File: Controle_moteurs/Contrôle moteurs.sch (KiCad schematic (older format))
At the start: 70 parts, among them P1 CONN_1, P10 CONN_1, P11 CONN_2, P12 CONN_2, P13 CONN_2, P14 CONN_2, P15 CONN_2, P16 CONN_2, P17 CONN_4, P18 CONN_5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

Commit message: Modification du connecteur de programmation
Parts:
- removed P16: CONN_2, symbol CONN_2
- removed P20: CONN_6, symbol CONN_6
- added P20, P21: CONN_5, symbol CONN_5
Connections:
- no-connect marks 0 -> 2
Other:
- note removed: "Connecteur debuggage"
- moved on the sheet: P9

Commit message: Renommé DEBUG_1/2 en TX et RX
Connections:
- net DEBUG_1 renamed DEBUG_TX
- net DEBUG_2 renamed DEBUG_RX
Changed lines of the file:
@@
-EESchema Schematic File Version 2  date 30/01/2018 12:00:08
+EESchema Schematic File Version 2  date 30/01/2018 14:31:43
 LIBS:power
 LIBS:device
@@
 $EndComp
 Text Label 10250 5850 2    60   ~ 0
-DEBUG_2
+DEBUG_RX
 Text Label 10250 5750 2    60   ~ 0
-DEBUG_1
+DEBUG_TX
 Text Notes 2200 6700 0    60   ~ 0
 Témoins d'alimentation
@@
 Need détrompeurs\nPlusieurs capas au lieu d'1 grosse
 Text Label 10400 3550 2    60   ~ 0
-DEBUG_2
+DEBUG_RX
 Text Label 10400 3450 2    60   ~ 0
-DEBUG_1
+DEBUG_TX
 Text Label 10400 4150 2    60   ~ 0
 RB4

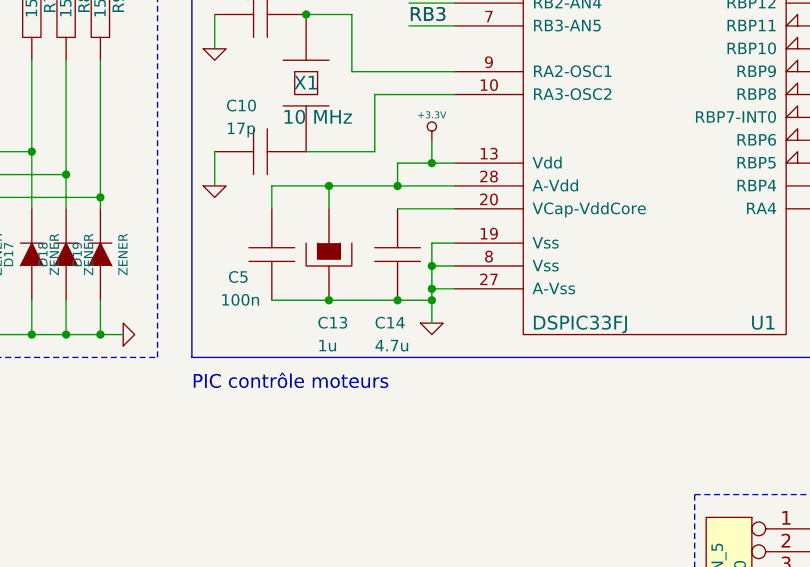
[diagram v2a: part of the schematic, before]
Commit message: Correctif : condensateur 4.7u n'était pas en polarisé
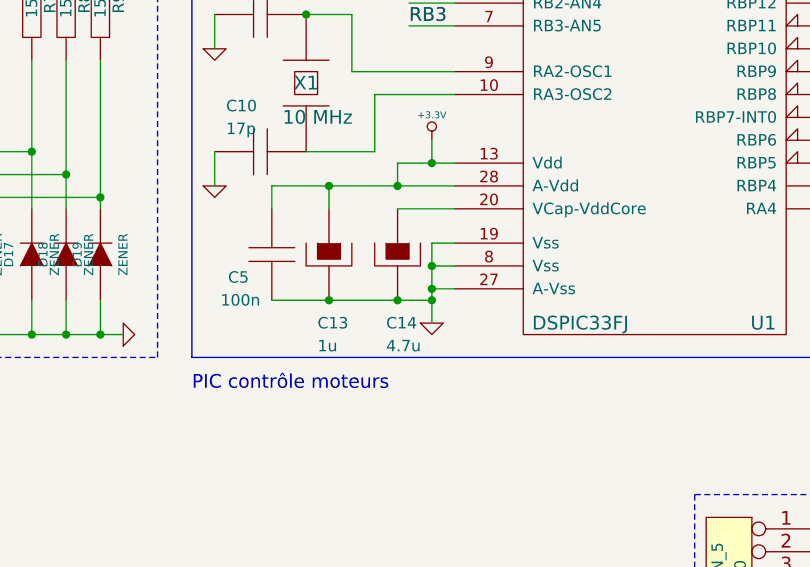
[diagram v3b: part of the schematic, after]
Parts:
- removed C14: 4.7u, symbol C
- added C14: 4.7u, symbol CAPAPOL
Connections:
- net GND: now also C14.2
- net at U1.20 (VCap-VddCore): now also C14.1
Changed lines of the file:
@@
-EESchema Schematic File Version 2  date 30/01/2018 14:31:43
+EESchema Schematic File Version 2  date 30/01/2018 16:42:31
 LIBS:power
 LIBS:device
@@
 Comment4 ""
 $EndDescr
+$Comp
+L CAPAPOL C14
+U 1 1 5A709251
+P 7900 4450
+F 0 "C14" H 7850 4150 50  0000 L CNN
+F 1 "4.7u" H 7850 4050 50  0000 L CNN
+	1    7900 4450
+	1    0    0    -1
+$EndComp
 Connection ~ 3700 1550
 Wire Wire Line
@@
 	1    0    0    -1
 $EndComp
-$Comp
-L C C14
-U 1 1 4BFD3B62
-P 7900 4450
-F 0 "C14" H 7800 4150 50  0000 L CNN
-F 1 "4.7u" H 7800 4050 50  0000 L CNN
-	1    7900 4450
-	1    0    0    -1
-$EndComp

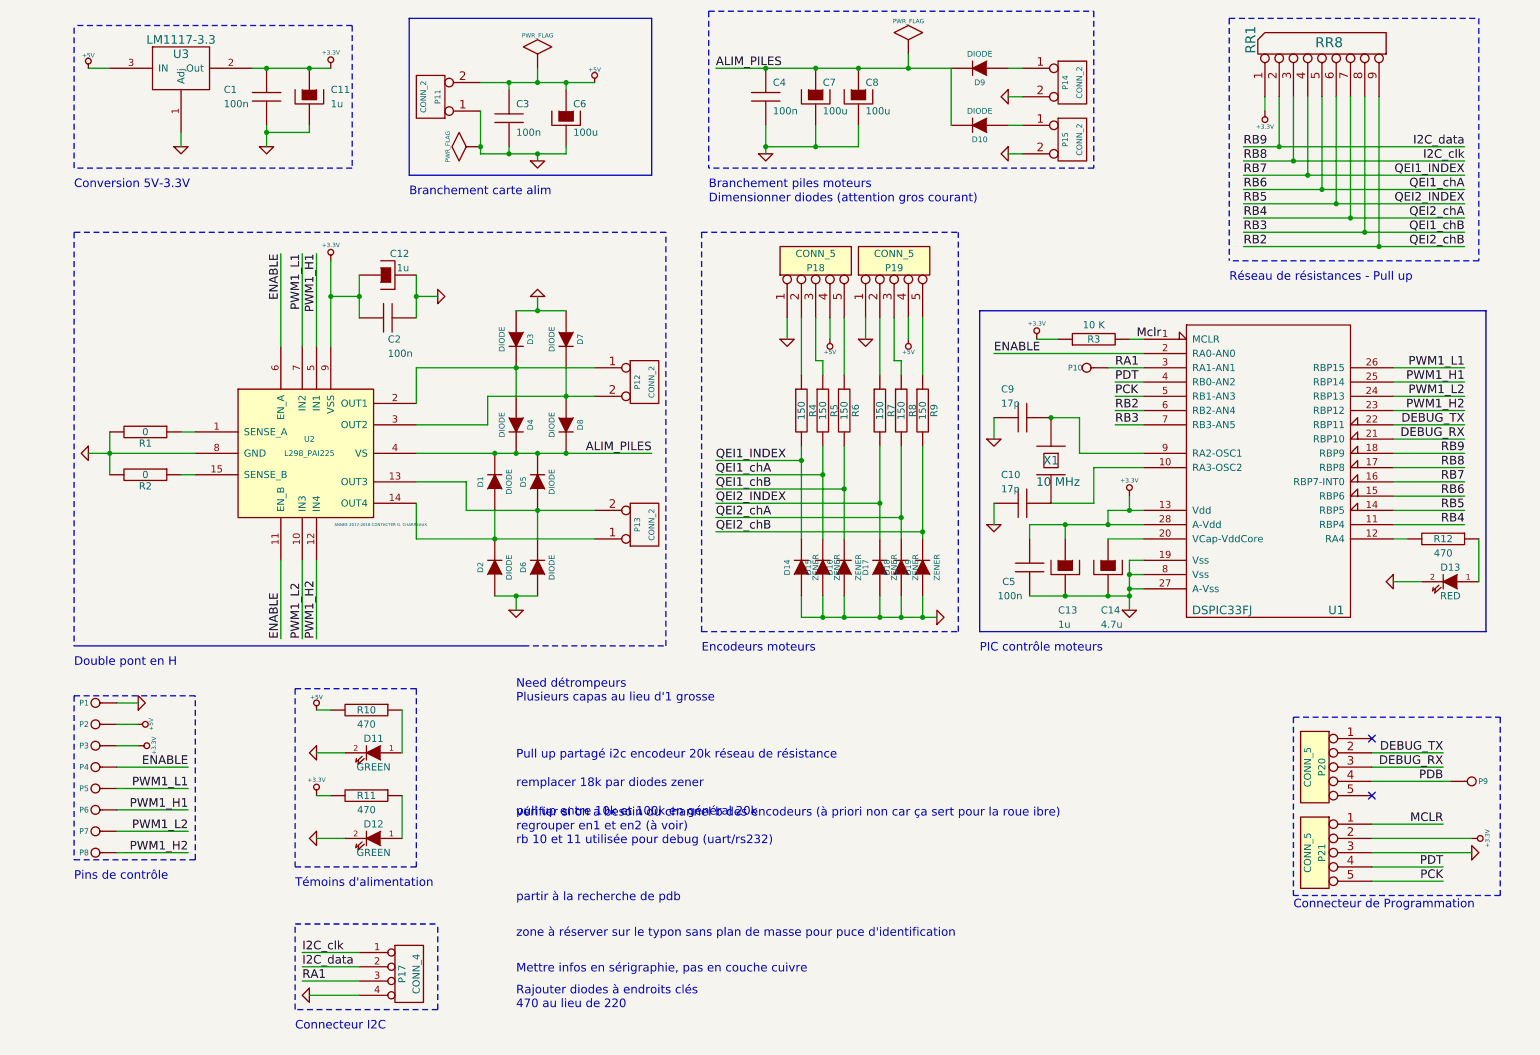
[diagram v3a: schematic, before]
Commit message: Modification connecteur programmation
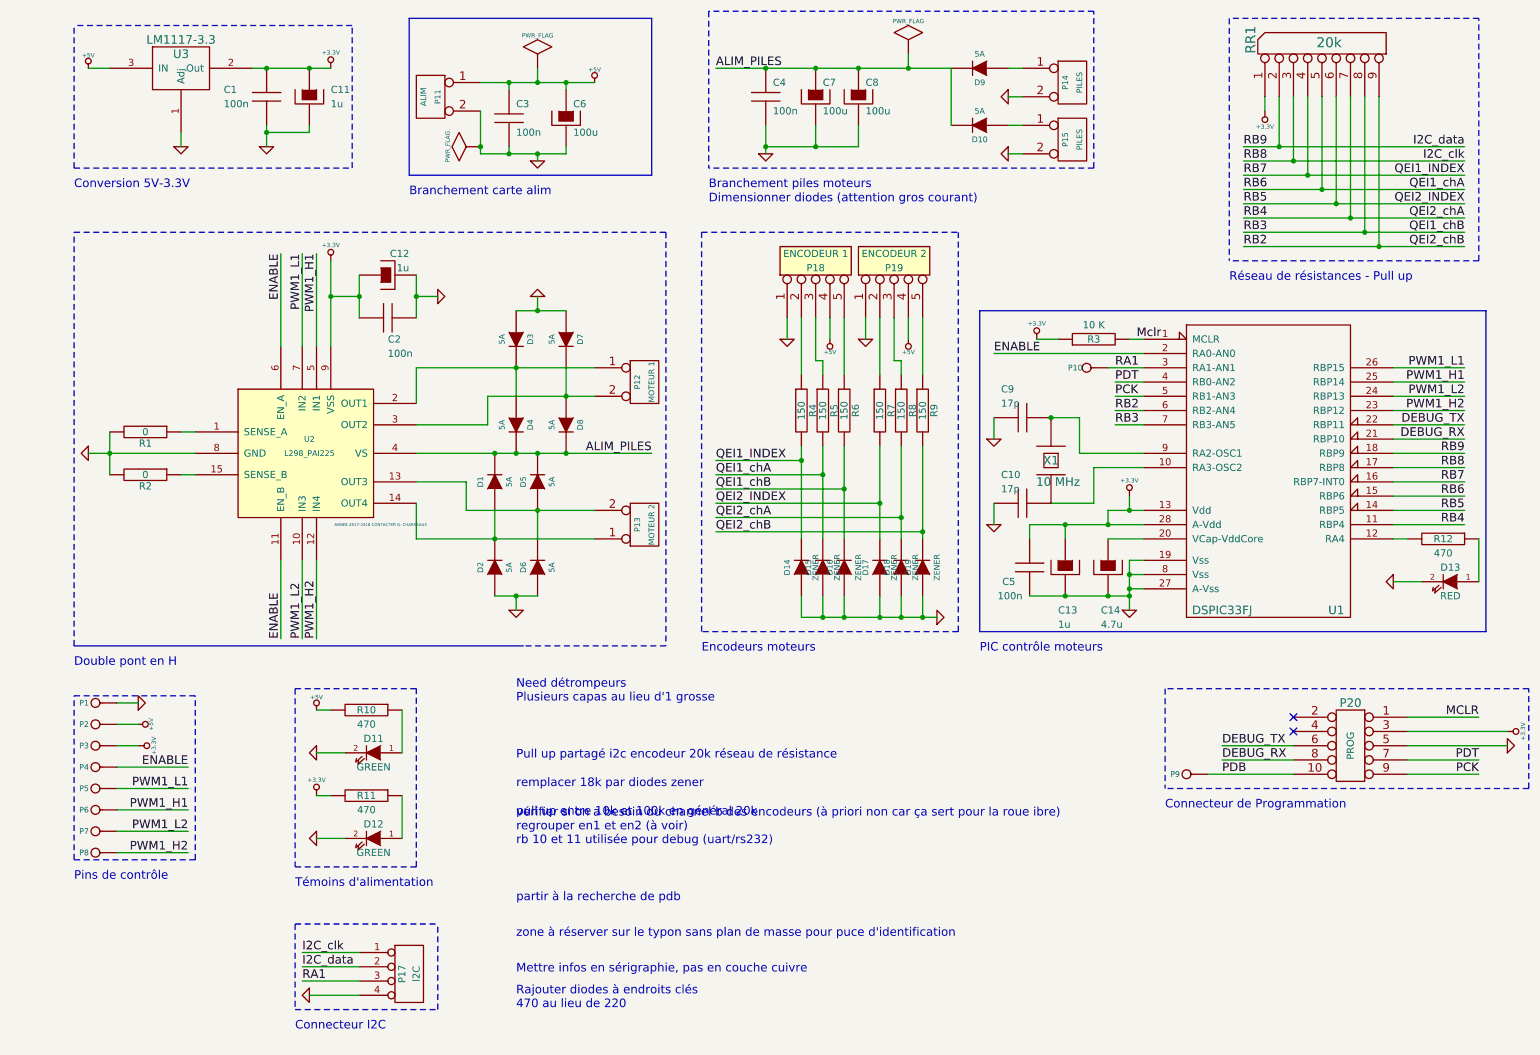
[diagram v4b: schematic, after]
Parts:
- removed P20, P21: CONN_5, symbol CONN_5
- added P20: PROG, symbol CONN_5X2
- D1, D10, D2, D3, D4, D5, D6, D7, D8, D9: value DIODE -> 5A
- P1: value CONN_1 -> GND
- P11: value CONN_2 -> ALIM
- P12: value CONN_2 -> MOTEUR 1
- P13: value CONN_2 -> MOTEUR 2
- P14, P15: value CONN_2 -> PILES
- P17: value CONN_4 -> I2C
- P18: value CONN_5 -> ENCODEUR 1
- P19: value CONN_5 -> ENCODEUR 2
- P2: value CONN_1 -> 5V
- P3: value CONN_1 -> 3.3V
- P4: value CONN_1 -> EN
- P5: value CONN_1 -> L1
- P6: value CONN_1 -> H1
- P7: value CONN_1 -> L2
- P8: value CONN_1 -> H2
- RR1: value RR8 -> 20k
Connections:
- net +3.3V: now also P20.3
- net +5V: now also P11.1 (P1); no longer P11.2 (PM)
- net DEBUG_RX: now also P20.8
- net DEBUG_TX: now also P20.6
- net GND: now also P11.2 (PM), P20.5; no longer P11.1 (P1)
- net MCLR: now also P20.1
- net PCK: now also P20.9
- net PDB: now also P20.10
- net PDT: now also P20.7
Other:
- moved on the sheet: P9

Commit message: Ajout des trous de fixation
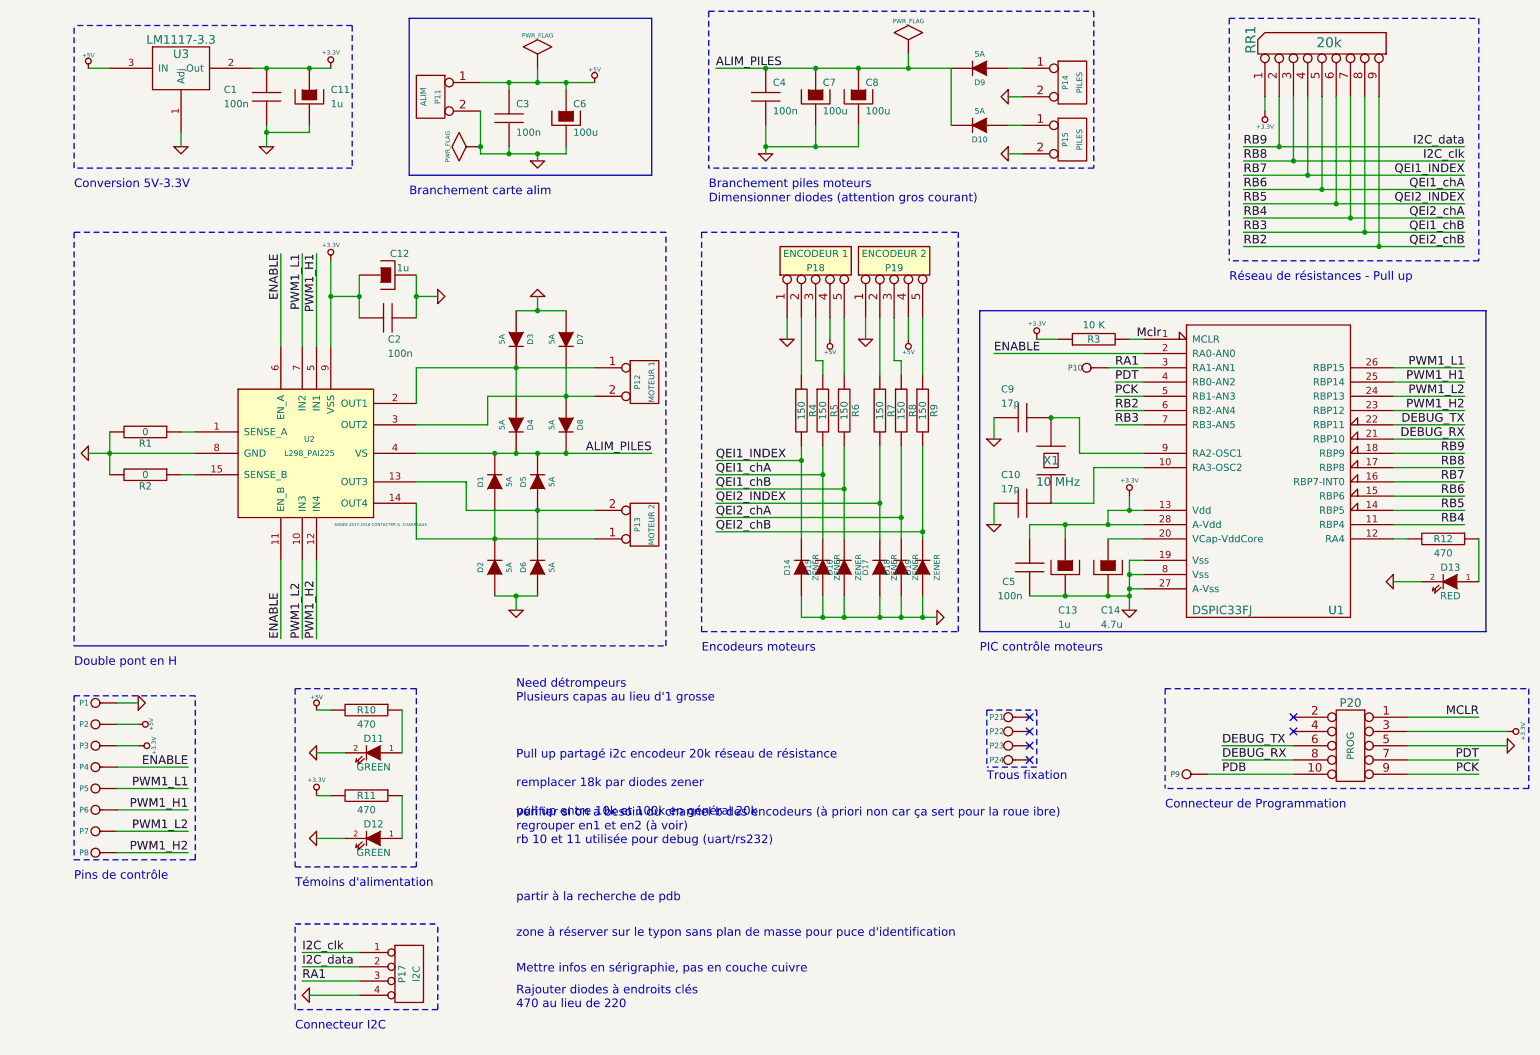
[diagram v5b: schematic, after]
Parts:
- added P21, P22, P23, P24: Fixe, symbol CONN_1
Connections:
- no-connect marks 2 -> 6
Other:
- note added: "Trous fixation"
